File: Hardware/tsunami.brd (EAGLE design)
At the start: 74.9 x 73.7 mm, 158 parts, among them J1 VDC-IN, J10 TRIG2, J11 TRIG1, J12 USD-SDIO-SOCKET, J13 GND, J14 AUDIO I/O, J15 MIDI, J2 GND-IN, J3 DEBUG, J4 USB-MICROB", J5 CORTEX_DEBUGPTH, J6 3.3VA, J7 3.3V, J8 PLAYING, J9 FTDI_DEVICE, Q1 2.5A/30V, U1 LM1117, U2 LM1117, U3 ATSAMS70N20A-AN, U4 AK4618VQSFE-PACKAGE, U5 74AHC1G125, U6 6N138M, Y1 11.2896 MHz

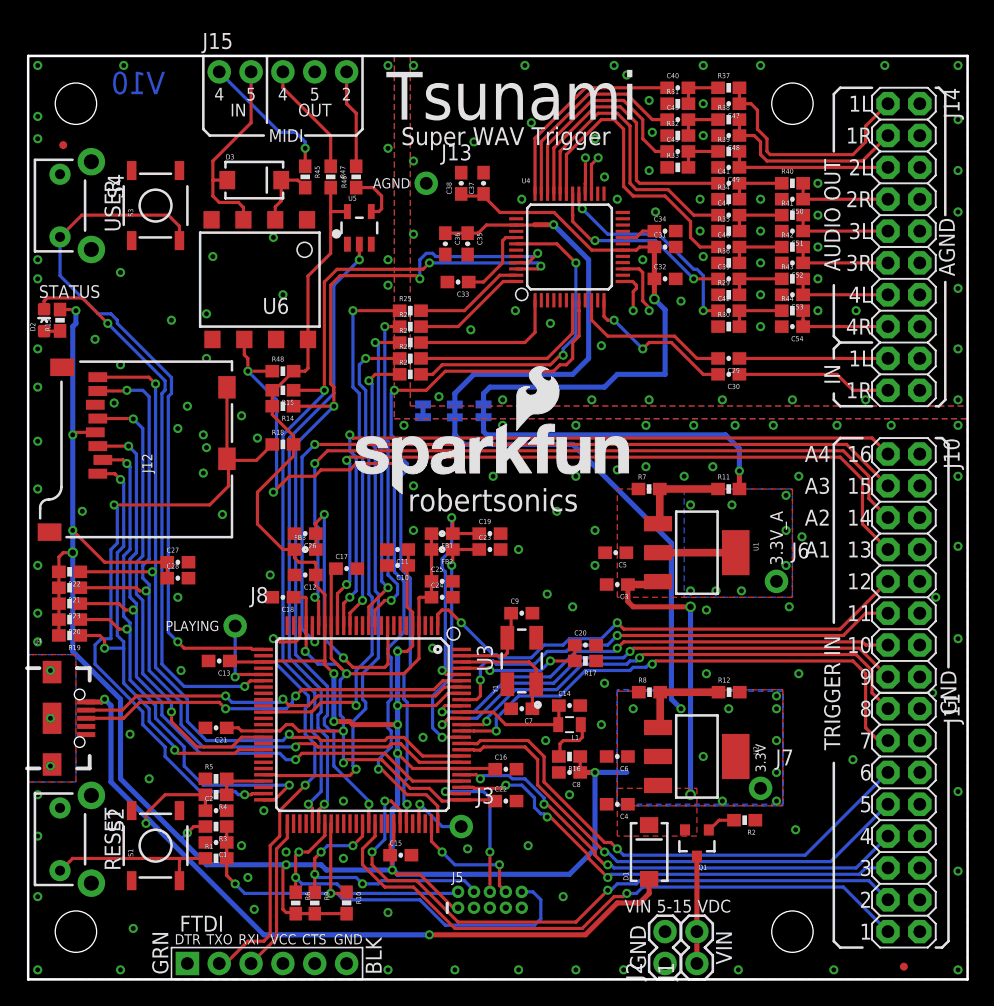
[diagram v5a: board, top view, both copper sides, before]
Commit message: Post review & production checklist.
-Centered staking vias on USB.
-Moved some vias to avoid silk.
-Text touchups around V reg outputs.
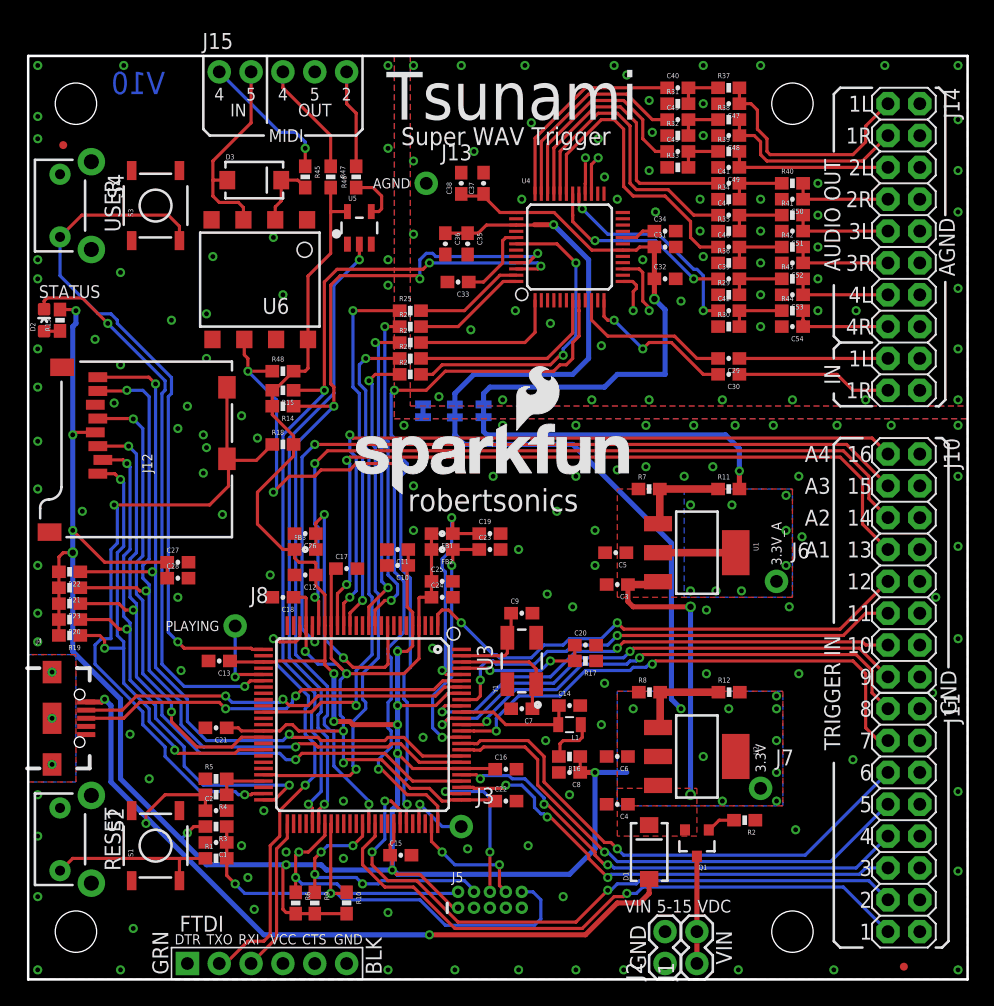
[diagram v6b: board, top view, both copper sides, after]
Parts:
- U4: value AK4618VQSFE-PACKAGE -> AK4618VQ
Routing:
- net GND: vias 166 -> 167
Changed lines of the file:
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@@
 <layer number="23" name="tOrigins" color="15" fill="1" visible="yes" active="yes"/>
 <layer number="24" name="bOrigins" color="15" fill="1" visible="no" active="yes"/>
-<layer number="25" name="tNames" color="7" fill="1" visible="yes" active="yes"/>
+<layer number="25" name="tNames" color="7" fill="1" visible="no" active="yes"/>
 <layer number="26" name="bNames" color="7" fill="1" visible="no" active="yes"/>
 <layer number="27" name="tValues" color="7" fill="1" visible="no" active="yes"/>
@@
 <text x="27.94" y="48.26" size="0.8128" layer="51" font="vector" ratio="15" align="center-right">TDMI</text>
 <text x="72.644" y="58.42" size="1.27" layer="21" font="vector" ratio="15" rot="R90" align="top-center">AGND</text>
-<text x="59.69" y="33.02" size="1.016" layer="21" font="vector" ratio="15" rot="R270" align="center-right">3.3V_A</text>
+<text x="59.69" y="33.02" size="0.8128" layer="21" font="vector" ratio="15" rot="R270" align="center-right">3.3V_A</text>
 <wire x1="72.39" y1="45.72" x2="72.644" y2="45.72" width="0.2032" layer="21"/>
 <wire x1="72.644" y1="45.72" x2="73.152" y2="46.228" width="0.2032" layer="21"/>
@@
 <wire x1="64.262" y1="51.308" x2="64.262" y2="55.372" width="0.2032" layer="22"/>
 <text x="72.644" y="58.42" size="1.27" layer="22" font="vector" ratio="15" rot="MR270" align="top-center">AGND</text>
-<text x="58.42" y="31.75" size="1.016" layer="22" font="vector" ratio="15" rot="MR180" align="center-right">3.3V_A</text>
+<text x="58.42" y="31.75" size="0.8128" layer="22" font="vector" ratio="15" rot="MR180" align="center-right">3.3V_A</text>
 <wire x1="72.39" y1="45.72" x2="72.644" y2="45.72" width="0.2032" layer="22"/>
 <wire x1="72.644" y1="45.72" x2="73.152" y2="46.228" width="0.2032" layer="22"/>
@@
 <wire x1="73.406" y1="3.048" x2="72.898" y2="2.54" width="0.2032" layer="21"/>
 <wire x1="72.898" y1="2.54" x2="72.39" y2="2.54" width="0.2032" layer="21"/>
-<text x="57.15" y="15.24" size="1.016" layer="22" font="vector" ratio="15" rot="MR0" align="center-left">3.3V</text>
+<text x="57.15" y="15.24" size="0.8128" layer="22" font="vector" ratio="15" rot="MR0" align="center-left">3.3V</text>
 <text x="38.608" y="68.58" size="3.81" layer="22" font="vector" ratio="15" rot="MR0" align="bottom-center">Tsunami</text>
 <text x="38.1" y="66.548" size="1.4224" layer="22" font="vector" ratio="15" rot="MR0" align="bottom-center">Super WAV Trigger</text>
@@
 <wire x1="64.262" y1="50.292" x2="64.262" y2="49.53" width="0.2032" layer="21"/>
 <wire x1="64.262" y1="46.736" x2="64.262" y2="46.228" width="0.2032" layer="21"/>
+<dimension x1="0" y1="11.176" x2="0" y2="0" x3="-7.874" y3="5.588" textsize="1.778" textratio="15" layer="47" unit="inch"/>
+<dimension x1="0" y1="61.722" x2="0" y2="0" x3="-21.082" y3="30.861" textsize="1.778" textratio="15" layer="47" unit="inch"/>
 </plain>
 <attributes>
@@
 <attribute name="PROD_ID" value="RES-00818" x="2.54" y="52.578" size="1.778" layer="27" rot="R90" display="off"/>
 </element>
-<element name="U4" library="tapestry" package="LQFP-48" value="AK4618VQSFE-PACKAGE" x="43.18" y="58.42">
+<element name="U4" library="tapestry" package="LQFP-48" value="AK4618VQ" x="43.18" y="58.42">
 <attribute name="PROD_ID" value="IC-13239" x="43.18" y="58.42" size="1.778" layer="27" display="off"/>
 </element>
@@
 <via x="45.974" y="64.008" extent="1-16" drill="0.381"/>
 <via x="46.99" y="62.23" extent="1-16" drill="0.381"/>
-<via x="45.212" y="67.056" extent="1-16" drill="0.381"/>
+<via x="45.466" y="67.056" extent="1-16" drill="0.381"/>
 <via x="49.022" y="57.404" extent="1-16" drill="0.381"/>
 <wire x1="31.496" y1="45.863" x2="31.496" y2="44.847" width="0.4064" layer="16"/>
@@
 <via x="30.734" y="65.278" extent="1-16" drill="0.381"/>
 <via x="30.734" y="72.898" extent="1-16" drill="0.381"/>
-<via x="35.56" y="66.802" extent="1-16" drill="0.381"/>
+<via x="35.56" y="66.04" extent="1-16" drill="0.381"/>
 <via x="39.624" y="72.898" extent="1-16" drill="0.381"/>
 <via x="46.736" y="72.898" extent="1-16" drill="0.381"/>
@@
 <via x="0.762" y="11.43" extent="1-16" drill="0.381"/>
 <via x="0.762" y="14.732" extent="1-16" drill="0.381"/>
+<via x="34.544" y="72.898" extent="1-16" drill="0.381"/>
 </signal>
 <signal name="N$1">
@@
 <vertex x="46.99" y="13.843"/>
 <vertex x="46.99" y="22.987"/>
-<vertex x="60.198" y="23.114"/>
+<vertex x="60.198" y="22.987"/>
 <vertex x="60.198" y="13.843"/>
 </polygon>
@@
 <wire x1="30.314" y1="33.02" x2="30.226" y2="32.932" width="0.254" layer="1"/>
 <wire x1="30.226" y1="32.932" x2="30.226" y2="29.718" width="0.254" layer="1"/>
-<polygon width="0.1778" layer="16">
-<vertex x="60.198" y="13.97"/>
-<vertex x="60.198" y="23.114"/>
-<vertex x="46.99" y="23.114"/>
-<vertex x="46.99" y="13.97"/>
-</polygon>
 <via x="53.848" y="17.78" extent="1-16" drill="0.381"/>
 <via x="59.69" y="14.224" extent="1-16" drill="0.381"/>
@@
 <contactref element="J4" pad="SHIELD3"/>
 <contactref element="J4" pad="SHIELD2"/>
-<via x="1.778" y="24.638" extent="1-16" drill="0.381"/>
-<via x="1.778" y="20.828" extent="1-16" drill="0.381"/>
-<via x="1.778" y="17.018" extent="1-16" drill="0.381"/>
+<via x="1.905" y="24.511" extent="1-16" drill="0.381"/>
+<via x="1.905" y="20.828" extent="1-16" drill="0.381"/>
+<via x="1.905" y="17.145" extent="1-16" drill="0.381"/>
 <polygon width="0.254" layer="16" isolate="0.3048">
 <vertex x="3.81" y="15.748"/>
